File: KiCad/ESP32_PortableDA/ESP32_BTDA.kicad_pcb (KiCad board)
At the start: 4 copper layers, 56 x 38 mm, 93 parts, among them J1 ASJ-200-B-HT, J2 USB_C_Receptacle_PowerOnly_6P, J3 JST_BattConn, J4 uart_conn, U1 PCM5100APWR, U2 TPA6133A2RTJR, U3 BQ25308RTER, U4 NCP177, U5 NCP177, U6 ESP32_D0WD_V3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

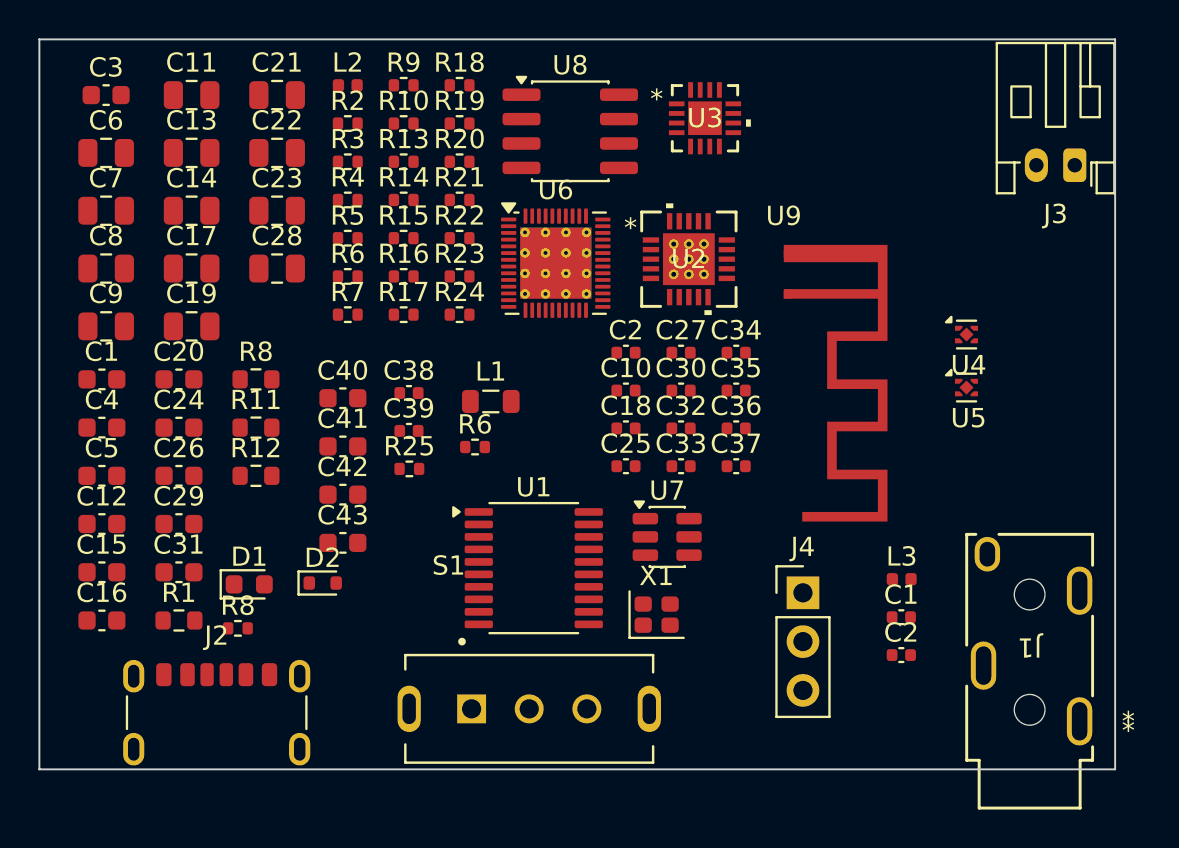
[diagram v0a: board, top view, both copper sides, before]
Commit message: Updated Schematic
added mounting holes, finished revision one, and unplaced/routed board (undone)
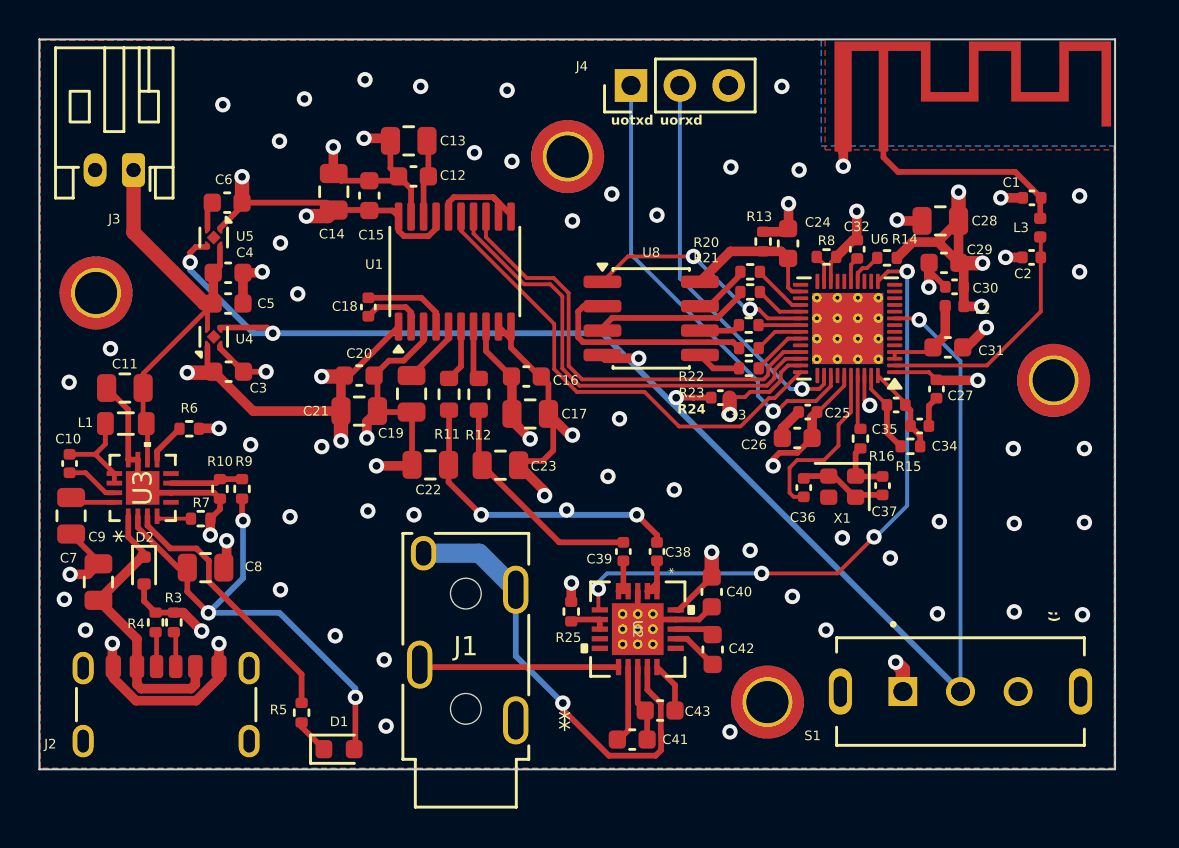
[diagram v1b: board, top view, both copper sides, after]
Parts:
- removed the C1 at (120.2, 90.4)
- removed the C2 at (147.5, 89.0)
- removed R1: R, Resistor_SMD:R_0603_1608Metric
- removed R17, R18, R19: 0, Resistor_SMD:R_0402_1005Metric
- removed R2: R, Resistor_SMD:R_0402_1005Metric
- removed the R6 at (133.0, 85.0)
- removed the R8 at (128.2, 90.4)
- removed U7: USBLC6-2SC6, Package_TO_SOT_SMD:SOT-23-6
- added H1: MountingHole, MountingHole:MountingHole_2.2mm_M2_DIN965_Pad_TopBottom, F.Cu at (154.8, 107.2)
- added H2: MountingHole, MountingHole:MountingHole_2.2mm_M2_DIN965_Pad_TopBottom, F.Cu at (119.9, 85.9)
- added H3: MountingHole, MountingHole:MountingHole_2.2mm_M2_DIN965_Pad_TopBottom, F.Cu at (144.4, 78.8)
- added H4: MountingHole, MountingHole:MountingHole_2.2mm_M2_DIN965_Pad_TopBottom, F.Cu at (169.8, 90.5)
- C6: footprint Capacitor_SMD:C_0805_2012Metric -> Capacitor_SMD:C_0603_1608Metric
- moved J3 49.0 mm to (121.8, 79.5)
- moved C29 42.1 mm to (164.0, 84.3), turned to 180 degrees
- moved C31 41.7 mm to (164.2, 88.7)
- moved U5 40.0 mm to (126.0, 83.0), turned to -90 degrees
- moved U4 39.2 mm to (126.0, 88.2), turned to 90 degrees
- moved R8 36.2 mm to (157.9, 84.0)
- moved U3 35.0 mm to (122.3, 96.1), turned to 90 degrees
- moved C28 34.6 mm to (163.8, 82.2), turned to 180 degrees
- moved L2 33.6 mm to (164.6, 86.6), turned to 180 degrees
- moved C24 33.1 mm to (155.9, 83.3), turned to 90 degrees
- moved C26 32.2 mm to (156.4, 93.5), turned to 180 degrees
- moved J1 29.4 mm to (141.8, 108.2)
- moved C10 29.2 mm to (118.5, 94.8), turned to 90 degrees
- moved R15 28.5 mm to (162.3, 93.9), turned to 180 degrees
- moved J4 27.9 mm to (147.8, 75.1), turned to 90 degrees
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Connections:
- net Net-(U2-TEST1) renamed /test
- net Net-(U3-TS) renamed /ts
- net Net-(U6-MTDI) renamed /mtdi
- C18 pad 1: /cap1 -> /capp
- U1 pad 10: /demp -> GND
- U1 pad 11: /flt -> GND
- U1 pad 16: /fmt -> GND
- U1 pad 2: /cap1 -> /capp
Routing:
- net VAA: track 0.00 -> 212.0 mm, vias 0 -> 13
- net GND: track 0.00 -> 123.1 mm, vias 0 -> 75
- net /en: track 0.00 -> 75.5 mm, vias 0 -> 3
- net VDD: track 0.00 -> 65.8 mm, vias 0 -> 3
- net /sd: track 0.00 -> 33.1 mm, vias 0 -> 4
- net /regn: track 0.00 -> 26.0 mm, vias 0 -> 3
- net /lrck: track 0.00 -> 25.2 mm
- net /din: track 0.00 -> 24.2 mm
- net /uotxd: track 0.00 -> 24.1 mm, vias 0 -> 1
- net /con_t: track 0.00 -> 23.7 mm, vias 0 -> 1
- net /bck: track 0.00 -> 23.6 mm
- net +BATT: track 0.00 -> 23.4 mm
- net /uorxd: track 0.00 -> 20.5 mm, vias 0 -> 1
- net /loutl: track 0.00 -> 16.2 mm, vias 0 -> 2
- net VBUS: track 0.00 -> 15.1 mm
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- added copper zone on B.Cu, net GND
- added copper zone on F.Cu, net GND
- added copper zone on In1.Cu, net GND
- added copper zone on F.Cu, net VAA
- added copper zone on In2.Cu, net VAA
- added copper zone on In2.Cu, net VDD
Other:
- rule pad_to_mask_clearance: 0 -> 0.1
- board text added: ";)"
- board text added: "Rev. 1.0"
- board text added: "uorxd"
- board text added: "uotxd"
